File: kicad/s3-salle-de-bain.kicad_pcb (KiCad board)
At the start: 2 copper layers, 100 x 80 mm, 0 parts

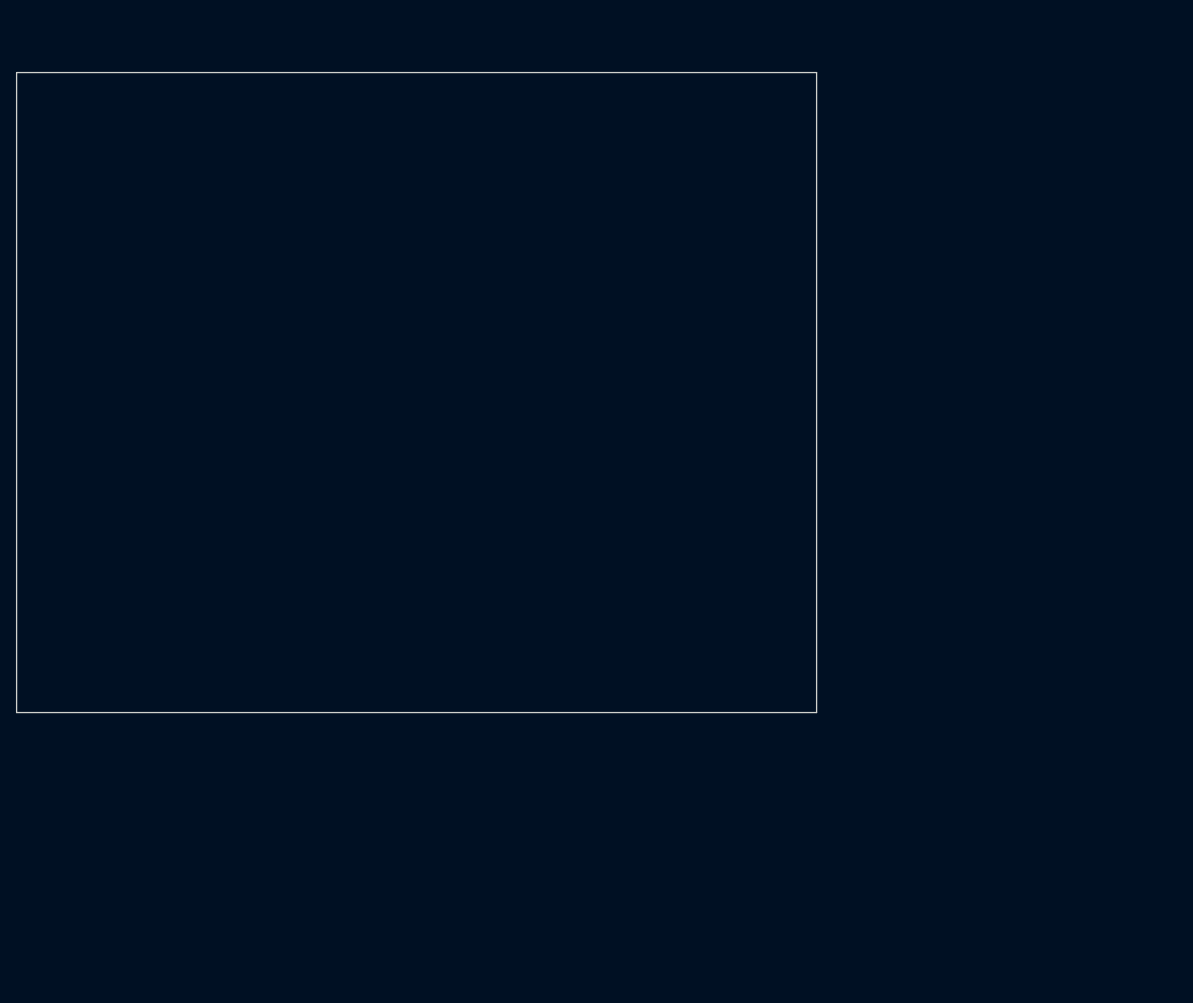
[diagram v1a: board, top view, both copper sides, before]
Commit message: feat(kicad): pre-populated PCB with 14 footprints + 23 nets connected
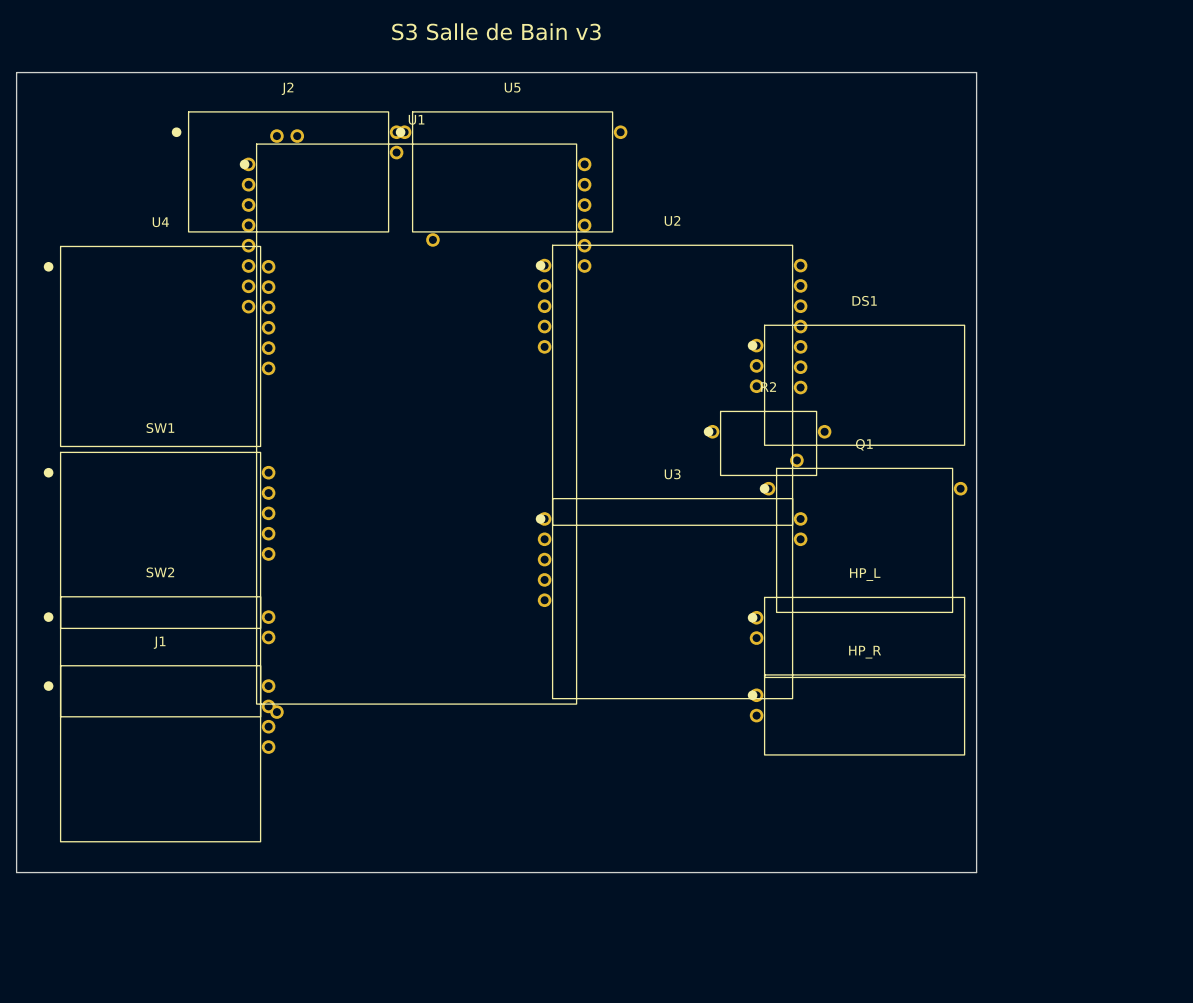
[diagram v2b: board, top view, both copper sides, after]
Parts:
- added DS1: WS2812 Ring x12, Generic:DS1_Module, F.Cu at (106.0, 39.1)
- added HP_L: HP gauche 40mm 4R 3W, Generic:HP_L_Module, F.Cu at (106.0, 70.6)
- added HP_R: HP droit 40mm 4R 3W, Generic:HP_R_Module, F.Cu at (106.0, 80.3)
- added J1: Jack 3.5mm, Generic:J1_Module, F.Cu at (18.0, 85.2)
- added J2: USB-C, Generic:J2_Module, F.Cu at (34.0, 12.4)
- added Q1: AO3401 P-MOS, Generic:Q1_Module, F.Cu at (106.0, 58.5)
- added R2: 330R, Generic:R2_Module, F.Cu at (94.0, 46.4)
- added SW1: Encodeur EC11, Generic:SW1_Module, F.Cu at (18.0, 58.5)
- added SW2: Switch mute SPDT, Generic:SW2_Module, F.Cu at (18.0, 73.0)
- added U1: ESP32-S3-DevKitC-1, Generic:U1_Module, F.Cu at (50.0, 43.9)
- added U2: PCM5102, Generic:U2_Module, F.Cu at (82.0, 39.1)
- added U3: PAM8403, Generic:U3_Module, F.Cu at (82.0, 65.8)
- added U4: INMP441, Generic:U4_Module, F.Cu at (18.0, 34.2)
- added U5: AMS1117-3.3, Generic:U5_Module, F.Cu at (62.0, 12.4)
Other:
- board size 100 x 80 mm -> 120 x 100 mm
- board text added: "S3 Salle de Bain v3"

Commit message: fix(pcb): real component footprints via pcbnew API (DRC clean)
- 22 real footprints from KiCad libs (SOT-223, SOT-23, EC11 encoder,
  PJ-320E jack, USB-C receptacle, SMD 0603/electrolytic, pin headers)
- 99 pads assigned to 23 nets, ratsnest ready to route
- DRC: 0 errors (edge clearance relaxed to 0.25mm for USB-C edge connector)
- Schematic symbols carry matching Footprint property (sch<->pcb linked)
- Verified with kicad-cli pcb drc + export
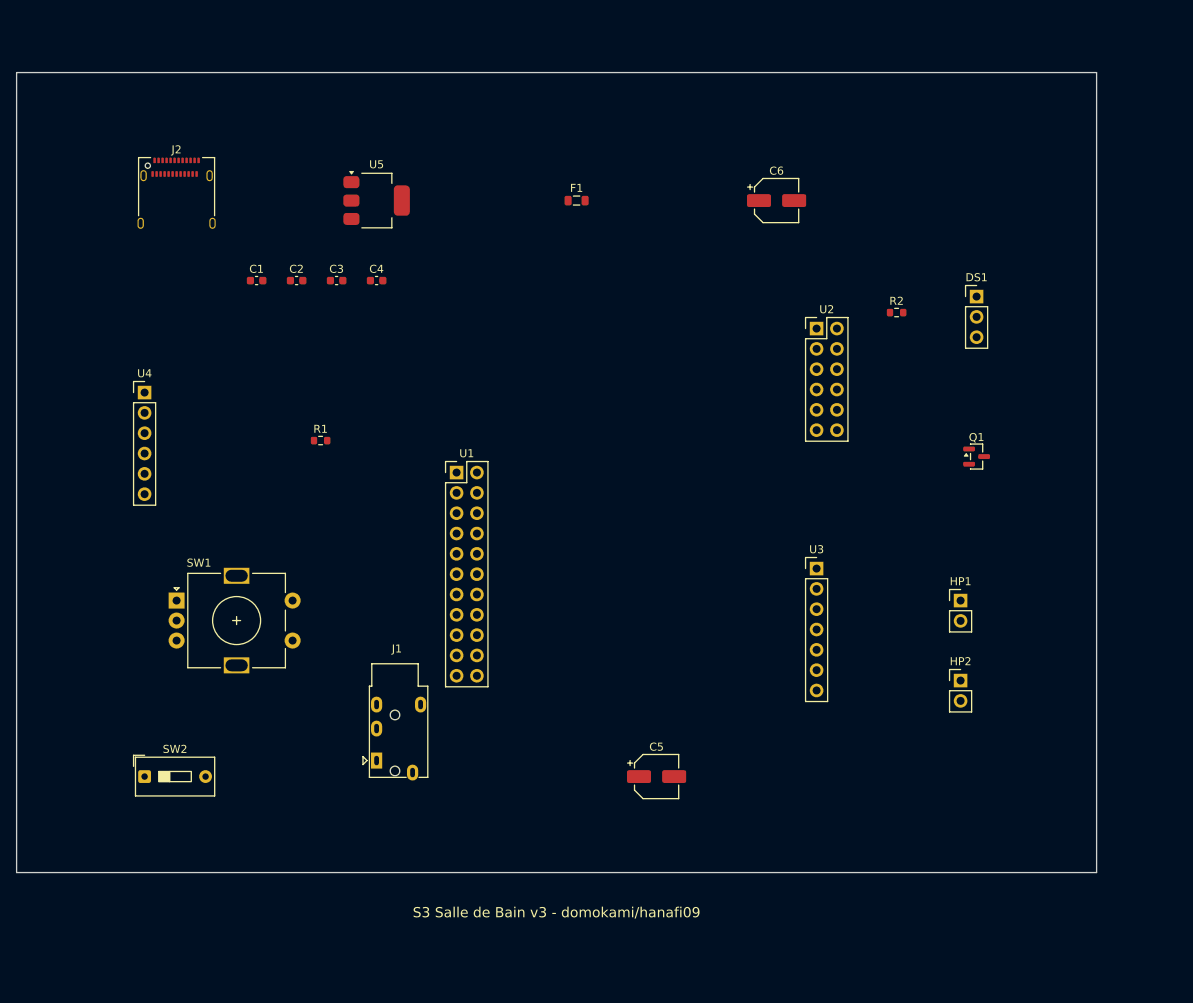
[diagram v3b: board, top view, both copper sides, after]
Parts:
- removed HP_L: HP gauche 40mm 4R 3W, Generic:HP_L_Module
- removed HP_R: HP droit 40mm 4R 3W, Generic:HP_R_Module
- added C1: 10uF, C_0603_1608Metric, F.Cu at (30.0, 26.0)
- added C2: 100nF, C_0603_1608Metric, F.Cu at (35.0, 26.0)
- added C3: 10uF, C_0603_1608Metric, F.Cu at (40.0, 26.0)
- added C4: 10uF, C_0603_1608Metric, F.Cu at (45.0, 26.0)
- added C5: 100uF, CP_Elec_5x5.3, F.Cu at (80.0, 88.0)
- added C6: 470uF, CP_Elec_5x5.3, F.Cu at (95.0, 16.0)
- added F1: Ferrite 600R, L_0805_2012Metric, F.Cu at (70.0, 16.0)
- added HP1: HP-Left, PinHeader_1x02_P2.54mm_Vertical, F.Cu at (118.0, 66.0)
- added HP2: HP-Right, PinHeader_1x02_P2.54mm_Vertical, F.Cu at (118.0, 76.0)
- added R1: 10k, R_0603_1608Metric, F.Cu at (38.0, 46.0)
- DS1: value WS2812 Ring x12 -> WS2812-Ring; footprint Generic:DS1_Module -> PinHeader_1x03_P2.54mm_Vertical
- J1: value Jack 3.5mm -> Jack-3.5mm; footprint Generic:J1_Module -> Jack_3.5mm_PJ320E_Horizontal
- J2: footprint Generic:J2_Module -> USB_C_Receptacle_Amphenol_12401610E4-2A
- Q1: value AO3401 P-MOS -> AO3401; footprint Generic:Q1_Module -> SOT-23
- R2: value 330R -> 330; footprint Generic:R2_Module -> R_0603_1608Metric
- SW1: value Encodeur EC11 -> EC11; footprint Generic:SW1_Module -> RotaryEncoder_Alps_EC11E-Switch_Vertical_H20mm
- SW2: value Switch mute SPDT -> Mute-SPDT; footprint Generic:SW2_Module -> SW_DIP_SPSTx01_Slide_9.78x4.72mm_W7.62mm_P2.54mm
- U1: footprint Generic:U1_Module -> PinHeader_2x11_P2.54mm_Vertical
- U2: footprint Generic:U2_Module -> PinHeader_2x06_P2.54mm_Vertical
- U3: footprint Generic:U3_Module -> PinHeader_1x07_P2.54mm_Vertical
- U4: footprint Generic:U4_Module -> PinHeader_1x06_P2.54mm_Vertical
- U5: footprint Generic:U5_Module -> SOT-223-3_TabPin2
- moved J1 27.0 mm to (45.0, 86.0)
- moved R2 22.9 mm to (110.0, 30.0)
- moved U2 19.3 mm to (100.0, 32.0)
- moved U3 18.4 mm to (100.0, 62.0)
- moved DS1 17.9 mm to (120.0, 28.0)
- moved Q1 17.5 mm to (120.0, 48.0)
- moved U5 17.4 mm to (45.0, 16.0)
- moved SW2 15.1 mm to (16.0, 88.0)
- moved J2 14.5 mm to (20.0, 16.0)
- moved U1 7.86 mm to (55.0, 50.0)
- moved SW1 7.78 mm to (20.0, 66.0)
- moved U4 6.10 mm to (16.0, 40.0)
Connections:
- U3 pad 6: SPK_L+ -> SPK_L
- U3 pad 7: SPK_R+ -> SPK_R
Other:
- board size 120 x 100 mm -> 135 x 100 mm
- board text added: "S3 Salle de Bain v3 - domokami/hanafi09"
- board text removed: "S3 Salle de Bain v3"

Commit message: fix(pcb): real ESP32-S3-DevKitC footprint (official Espressif)
- Download official Espressif ESP32-S3-DevKitC.kicad_mod (44 pads, 2x22)
- Map nets to exact GPIO pads per Espressif silk pinout
- Register Espressif.pretty in fp-lib-table
- Reposition all components around the larger module footprint
- DRC: 0 errors
- Schematic U1 footprint property -> Espressif:ESP32-S3-DevKitC
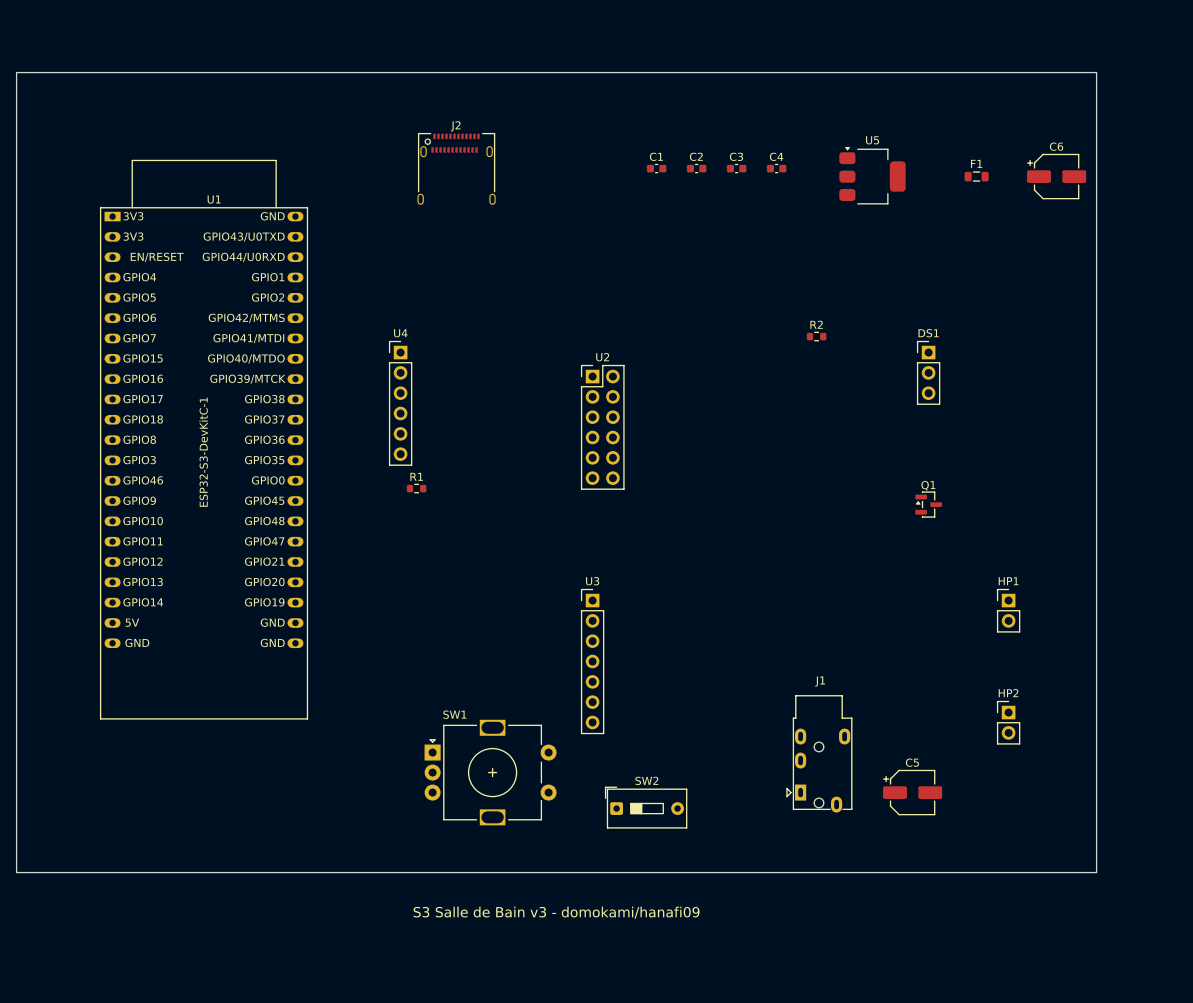
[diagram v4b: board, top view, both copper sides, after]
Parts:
- U1: footprint PinHeader_2x11_P2.54mm_Vertical -> ESP32-S3-DevKitC
- moved U5 62.1 mm to (107.0, 13.0)
- moved SW2 59.1 mm to (75.0, 92.0)
- moved U1 53.6 mm to (12.0, 18.0)
- moved J1 53.2 mm to (98.0, 90.0)
- moved C1 51.9 mm to (80.0, 12.0)
- moved C2 51.9 mm to (85.0, 12.0)
- moved C3 51.9 mm to (90.0, 12.0)
- moved C4 51.9 mm to (95.0, 12.0)
- moved F1 50.1 mm to (120.0, 13.0)
- moved SW1 37.2 mm to (52.0, 85.0)
- moved C6 35.1 mm to (130.0, 13.0)
- moved J2 35.1 mm to (55.0, 13.0)
- moved U4 32.4 mm to (48.0, 35.0)
- moved C5 32.1 mm to (112.0, 90.0)
- moved U2 28.6 mm to (72.0, 38.0)
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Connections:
- U1 pad 1: BTN_CENTER -> +3V3
- U1 pad 10: DAC_BCK -> JACK_DET
- U1 pad 11: DAC_DIN -> ENC_B
- U1 pad 12: LED_DIN_RAW -> DAC_BCK
- U1 pad 13: LED_PWR_EN -> (no net)
- U1 pad 14: AMP_EN -> (no net)
- U1 pad 15: +3V3 -> LED_PWR_EN
- U1 pad 16: +5V -> DAC_DIN
- U1 pad 17: GND -> MIC_DIN
- U1 pad 2: MUTE_SW -> (no net)
- U1 pad 21: (no net) -> +5V
- U1 pad 22: (no net) -> GND
- U1 pad 3: MIC_LRCLK -> (no net)
- U1 pad 4: MIC_BCLK -> MIC_LRCLK
- U1 pad 5: MIC_DIN -> MIC_BCLK
- U1 pad 6: ENC_A -> (no net)
- U1 pad 7: JACK_DET -> DAC_LRCK
- U1 pad 8: ENC_B -> (no net)
- U1 pad 9: DAC_LRCK -> ENC_A

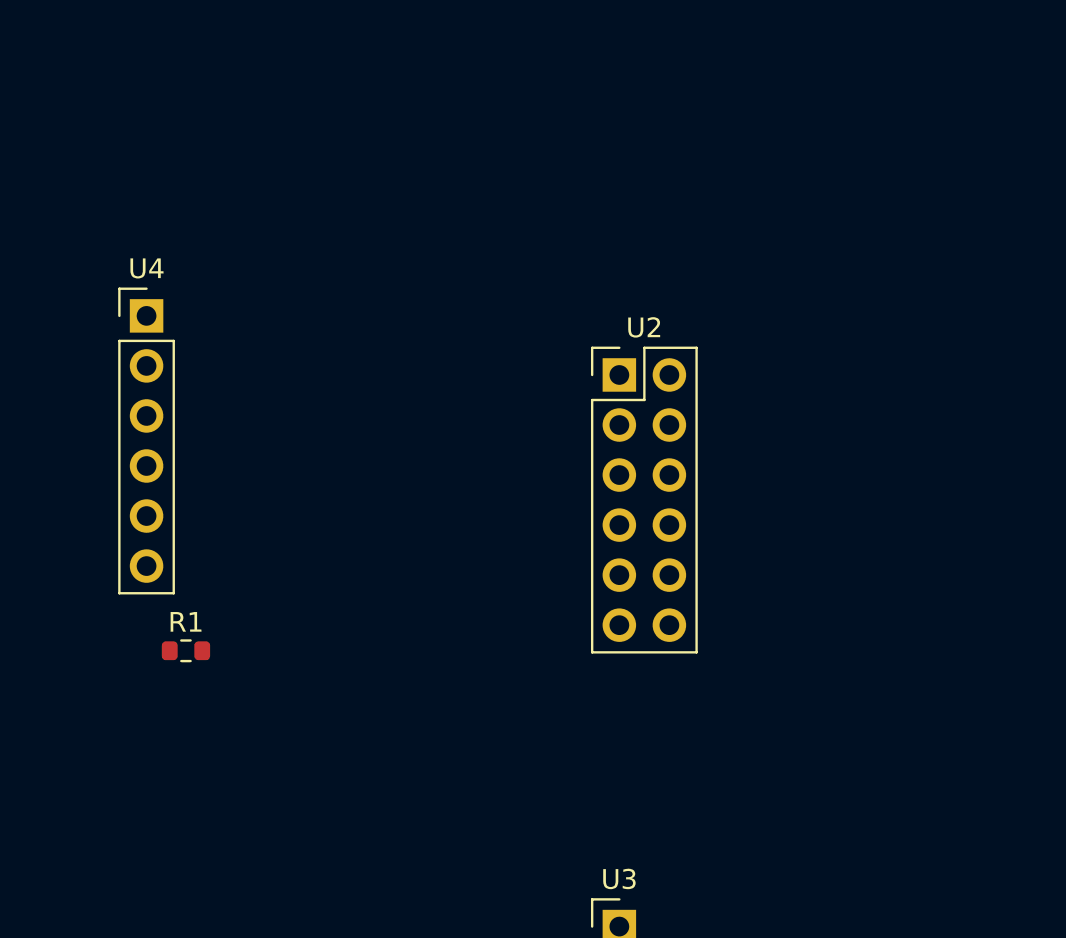
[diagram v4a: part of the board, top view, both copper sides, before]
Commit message: fix(pcb): real GY-PCM5102 module footprint (1x11 header + L/G/R)
- Custom footprint matching the WCMCU/GY-PCM5102 board (31.8x23.8mm)
- Pin order XMT FMT LCK DIN BCK SCL DMP FLT GND 3V3 VCC + L/G/R line-out
- Net mapping per module silk (SCL/DMP/FLT/FMT->GND, XMT->3V3)
- Schematic U2 symbol + footprint property updated to match
- Register Modules.pretty in fp-lib-table
- DRC: 0 errors
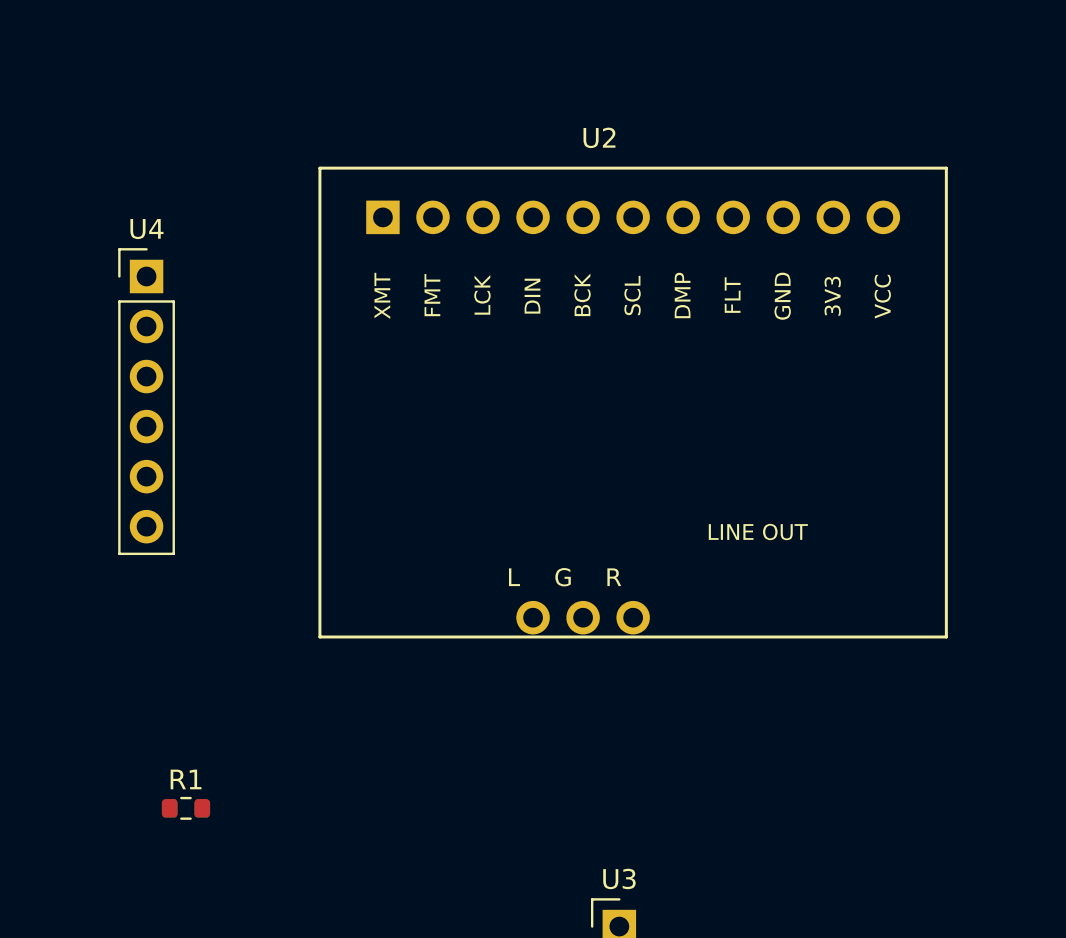
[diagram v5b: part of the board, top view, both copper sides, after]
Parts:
- U2: value PCM5102 -> GY-PCM5102; footprint PinHeader_2x06_P2.54mm_Vertical -> GY-PCM5102
- moved U2 14.4 mm to (60.0, 30.0)
- moved R1 8.00 mm to (50.0, 60.0)
- moved U4 2.00 mm to (48.0, 33.0)
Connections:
- U2 pad 11: AUDIO_L -> +3V3
- U2 pad 3: DAC_BCK -> DAC_LRCK
- U2 pad 5: DAC_LRCK -> DAC_BCK
